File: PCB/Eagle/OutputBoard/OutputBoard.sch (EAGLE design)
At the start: 10 parts, among them IC1 74LS138N

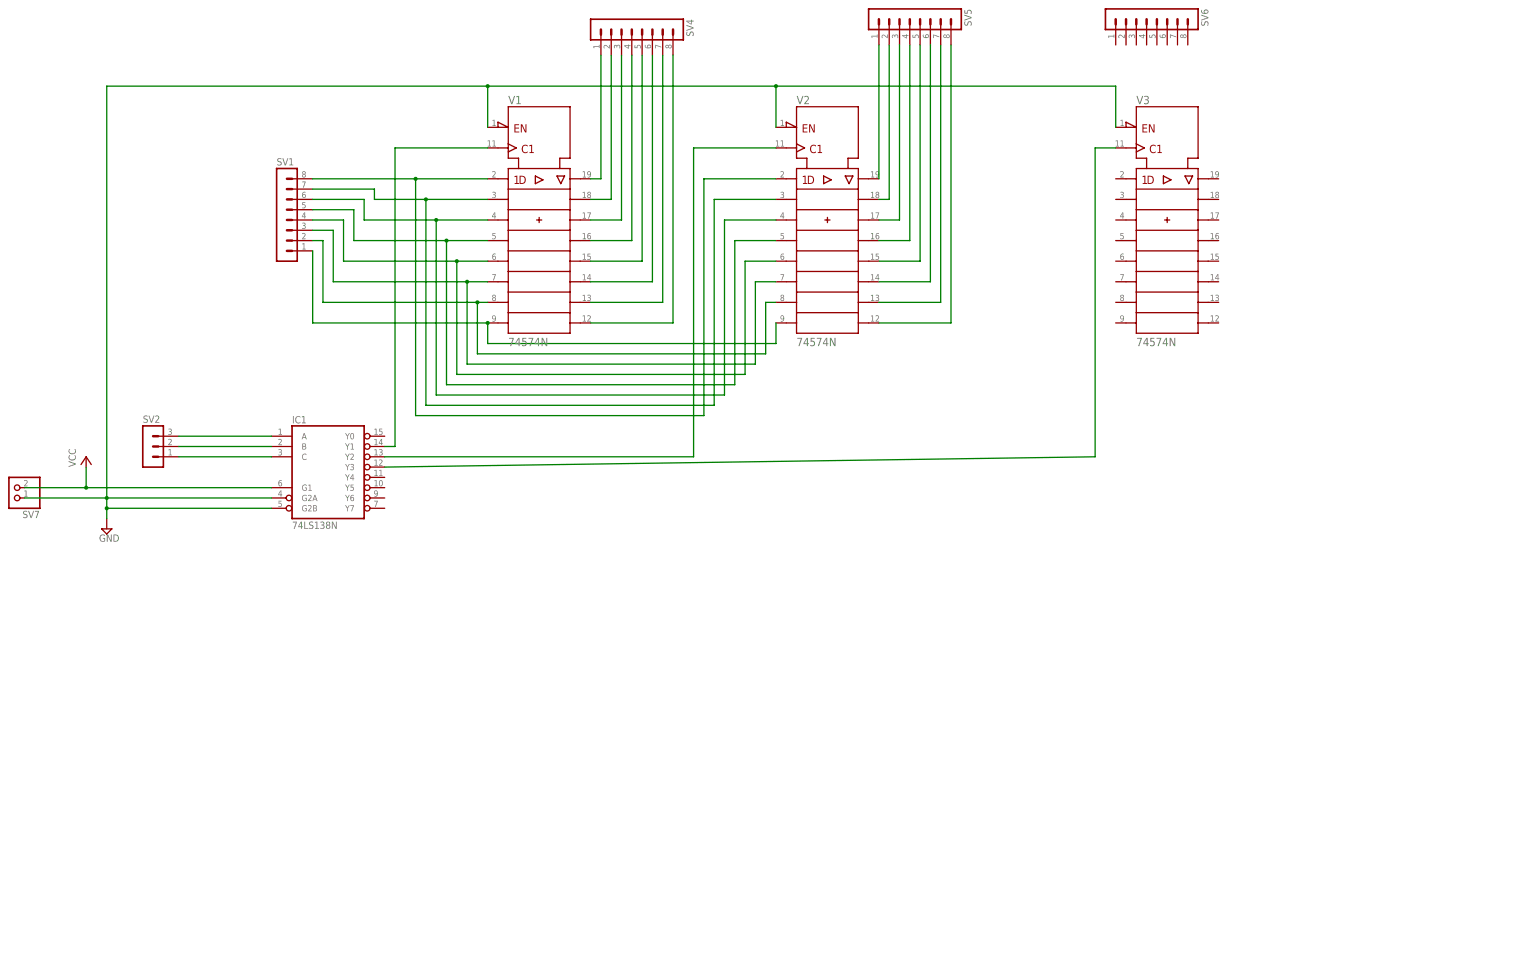
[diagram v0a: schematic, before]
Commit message: Blank display for IAS and updates in PCB boards
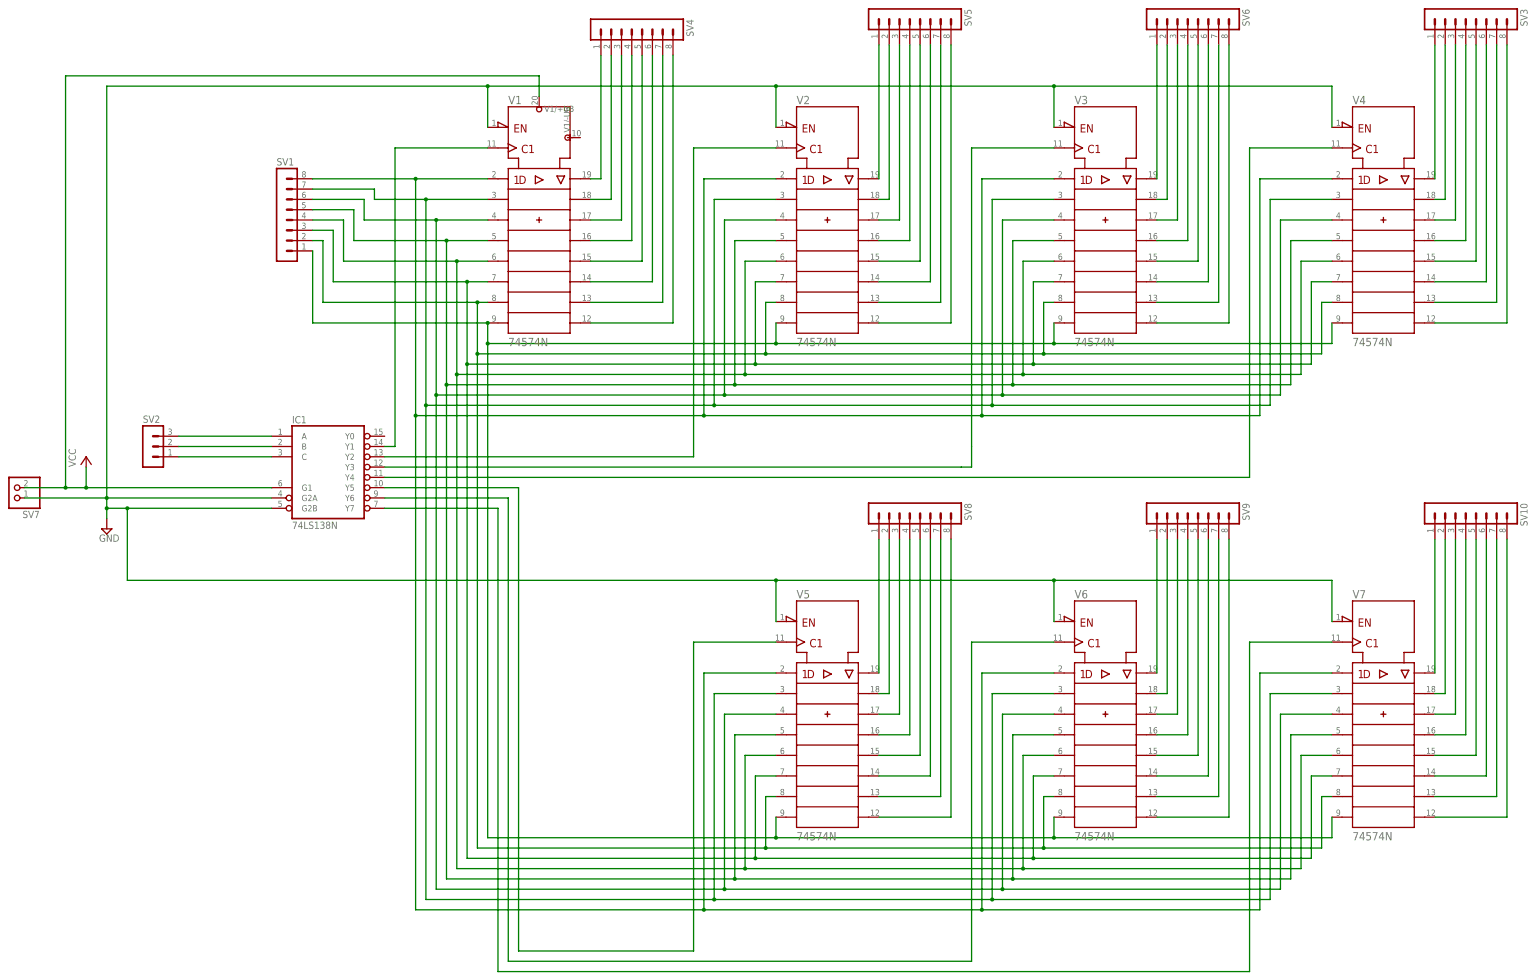
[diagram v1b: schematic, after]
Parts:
- added SV10, SV3, SV8, SV9: (no value), con-lstb:MA08-1
- added V4, V5, V6, V7: 74574N, 74ttl-din:74574N
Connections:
- removed net BUS0: SV1.8, V11.1D, V21.1D
- removed net DATA4: SV1.4, V11.5D, V21.5D
- removed net DATA5: SV1.3, V11.6D, V21.6D
- removed net DATA6: SV1.2, V11.7D, V21.7D
- removed net DATA7: SV1.1, V11.8D, V21.8D
- removed net N$13: SV1.7, V11.2D, V21.2D
- removed net N$14: SV1.6, V11.3D, V21.3D
- removed net N$15: SV1.5, V11.4D, V21.4D
- new net BUS1: SV1.8, V11.1D, V21.1D, V31.1D, V41.1D, V51.1D, V61.1D, V71.1D
- new net DATA1: SV1.1, V11.8D, V21.8D, V31.8D, V41.8D, V51.8D, V61.8D, V71.8D
- new net DATA2: SV1.2, V11.7D, V21.7D, V31.7D, V41.7D, V51.7D, V61.7D, V71.7D
- new net DATA3: SV1.3, V11.6D, V21.6D, V31.6D, V41.6D, V51.6D, V61.6D, V71.6D
- new net DATA8: SV1.4, V11.5D, V21.5D, V31.5D, V41.5D, V51.5D, V61.5D, V71.5D
- new net N$26: IC1A.Y4, V41.CLK
- new net N$27: IC1A.Y5, V51.CLK
- new net N$28: IC1A.Y6, V61.CLK
- new net N$29: SV1.7, V11.2D, V21.2D, V31.2D, V41.2D, V51.2D, V61.2D, V71.2D
- new net N$30: SV6.1, V31.1Q
- new net N$31: SV6.2, V31.2Q
- new net N$32: SV6.3, V31.3Q
- new net N$33: SV6.4, V31.4Q
- new net N$34: SV6.5, V31.5Q
- new net N$35: SV6.6, V31.6Q
- new net N$36: SV6.7, V31.7Q
- new net N$37: SV6.8, V31.8Q
- new net N$38: SV3.1, V41.1Q
- new net N$39: SV3.2, V41.2Q
- new net N$40: SV3.3, V41.3Q
- new net N$41: SV3.4, V41.4Q
- new net N$42: SV3.5, V41.5Q
- new net N$43: SV3.6, V41.6Q
- new net N$44: SV3.7, V41.7Q
- new net N$45: SV3.8, V41.8Q
- new net N$46: SV1.6, V11.3D, V21.3D, V31.3D, V41.3D, V51.3D, V61.3D, V71.3D
- new net N$47: SV1.5, V11.4D, V21.4D, V31.4D, V41.4D, V51.4D, V61.4D, V71.4D
- new net N$48: SV8.1, V51.1Q
- new net N$49: SV8.2, V51.2Q
- new net N$50: SV8.3, V51.3Q
- new net N$51: SV8.4, V51.4Q
- new net N$52: SV8.5, V51.5Q
- new net N$53: SV8.6, V51.6Q
- new net N$54: SV8.7, V51.7Q
- new net N$55: SV8.8, V51.8Q
- new net N$56: SV9.1, V61.1Q
- new net N$57: SV9.2, V61.2Q
- new net N$58: SV9.3, V61.3Q
- new net N$59: SV9.4, V61.4Q
- new net N$60: SV9.5, V61.5Q
- new net N$61: SV9.6, V61.6Q
- new net N$62: SV9.7, V61.7Q
- new net N$63: SV9.8, V61.8Q
- new net N$64: IC1A.Y7, V71.CLK
- new net N$65: SV10.1, V71.1Q
- new net N$66: SV10.2, V71.2Q
- new net N$67: SV10.3, V71.3Q
- new net N$68: SV10.4, V71.4Q
- new net N$69: SV10.5, V71.5Q
- new net N$70: SV10.6, V71.6Q
- new net N$71: SV10.7, V71.7Q
- new net N$72: SV10.8, V71.8Q
- net GND: now also V41.!OC, V51.!OC, V61.!OC, V71.!OC
- net VCC: now also V1/+UB.+UB
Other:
- moved on the sheet: SV6, V3

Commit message: New InputBoard and some modifications to OutputBoard
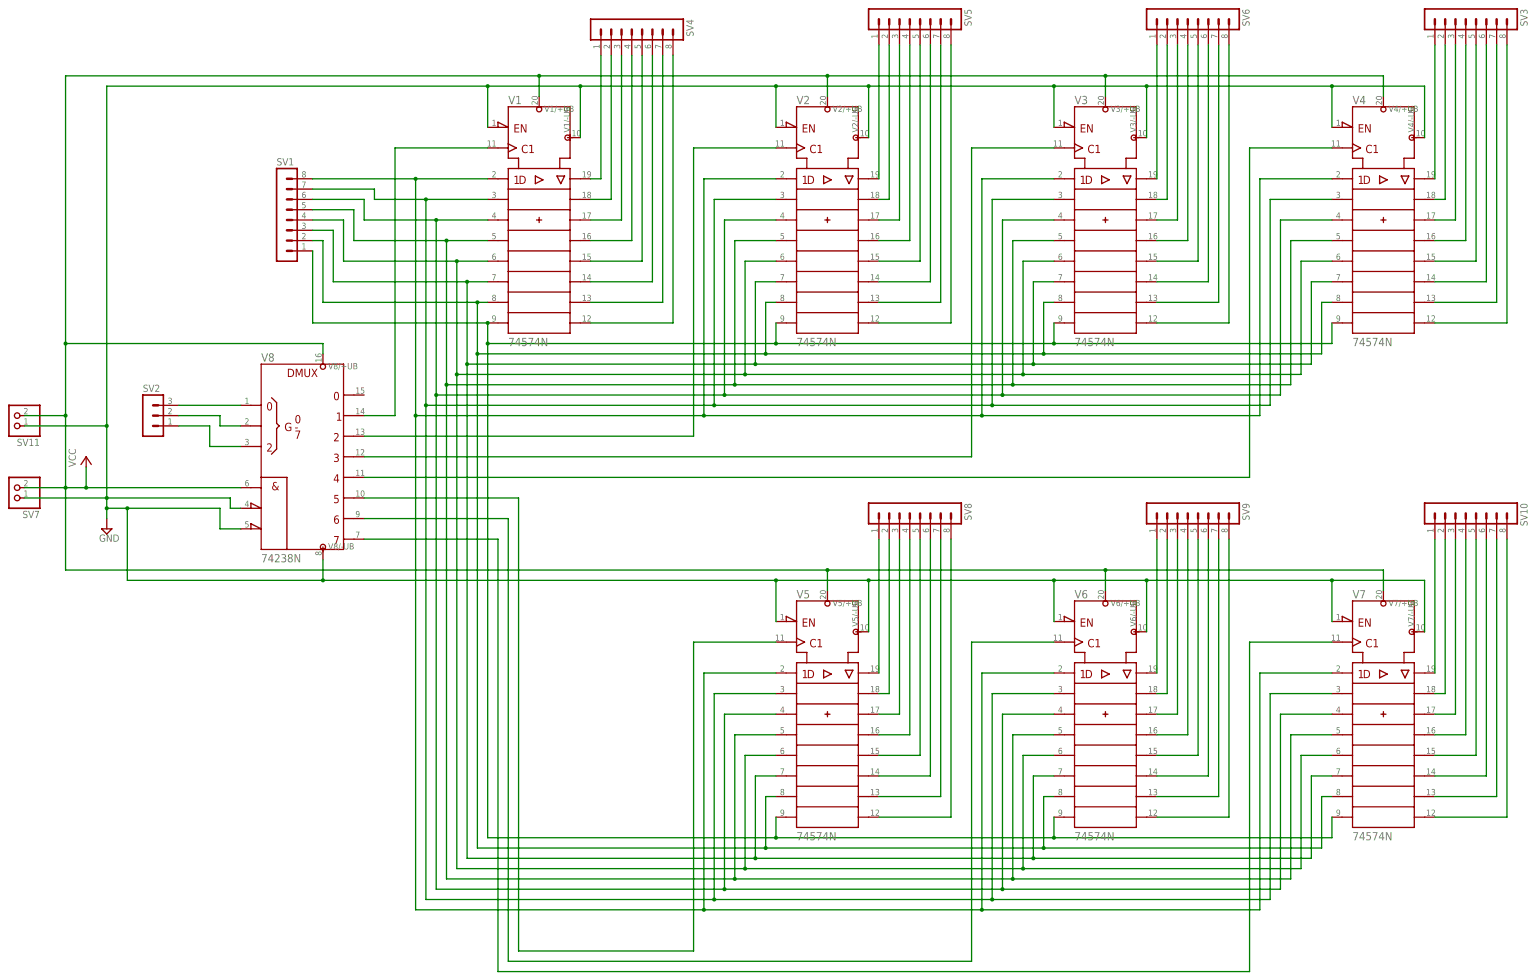
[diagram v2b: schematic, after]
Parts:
- removed IC1: 74LS138N, 74xx-us:74LS138N
- added SV11: (no value), pinhead:PINHD-1X2
- added V8: 74238N, 74ttl-din:74238N
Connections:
- removed net N$21: IC1A.B, SV2.2
- removed net N$22: IC1A.C, SV2.1
- new net N$13: SV2.2, V81.B
- new net N$14: SV2.1, V81.C
- net GND: now also SV11.1, V1/-UB.-UB, V2/-UB.-UB, V3/-UB.-UB, V4/-UB.-UB, V5/-UB.-UB, V6/-UB.-UB, V7/-UB.-UB, V8/-UB.-UB, V81.!G2A, V81.!G2B; no longer IC1A.G2A, IC1A.G2B
- net N$1: now also V81.Y3; no longer IC1A.Y3
- net N$20: now also V81.A; no longer IC1A.A
- net N$26: now also V81.Y4; no longer IC1A.Y4
- net N$27: now also V81.Y5; no longer IC1A.Y5
- net N$28: now also V81.Y6; no longer IC1A.Y6
- net N$3: now also V81.Y1; no longer IC1A.Y1
- net N$4: now also V81.Y2; no longer IC1A.Y2
- net N$64: now also V81.Y7; no longer IC1A.Y7
- net VCC: now also SV11.2, V2/+UB.+UB, V3/+UB.+UB, V4/+UB.+UB, V5/+UB.+UB, V6/+UB.+UB, V7/+UB.+UB, V8/+UB.+UB, V81.G1; no longer IC1A.G1
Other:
- moved on the sheet: SV2
